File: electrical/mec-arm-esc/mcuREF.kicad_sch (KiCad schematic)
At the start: 15 parts, among them SW1 SH-1808SN-250GF, SW2 SH-1808SN-250GF, U2 STM32G474RET3

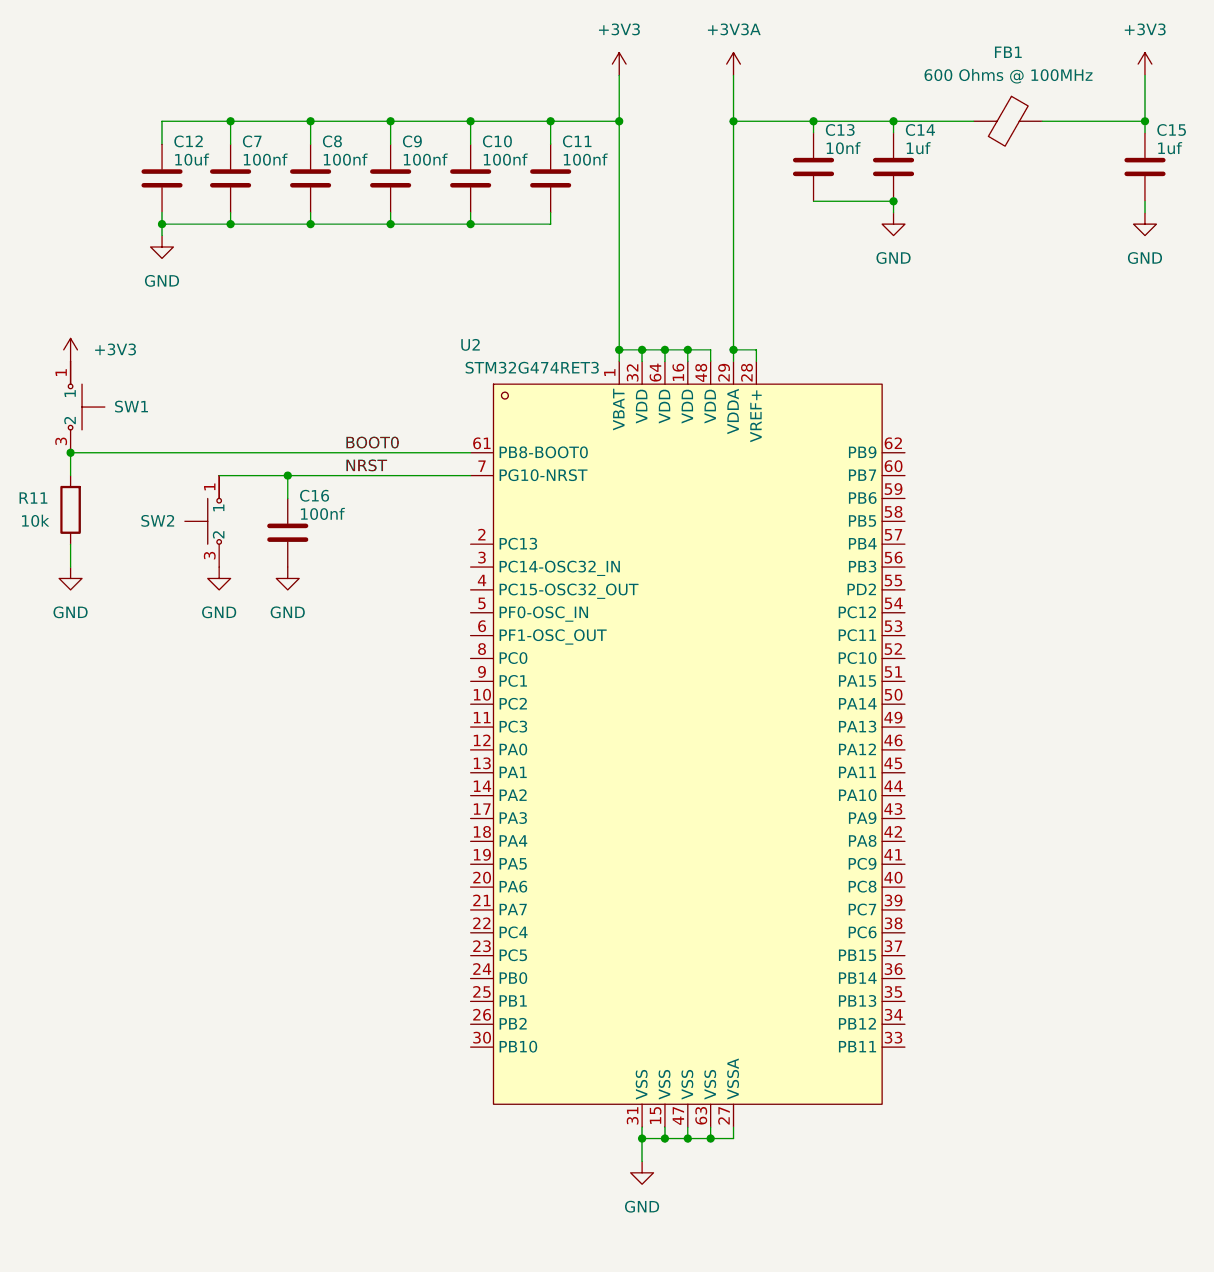
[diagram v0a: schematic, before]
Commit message: updated arm with proper basic mcu routing
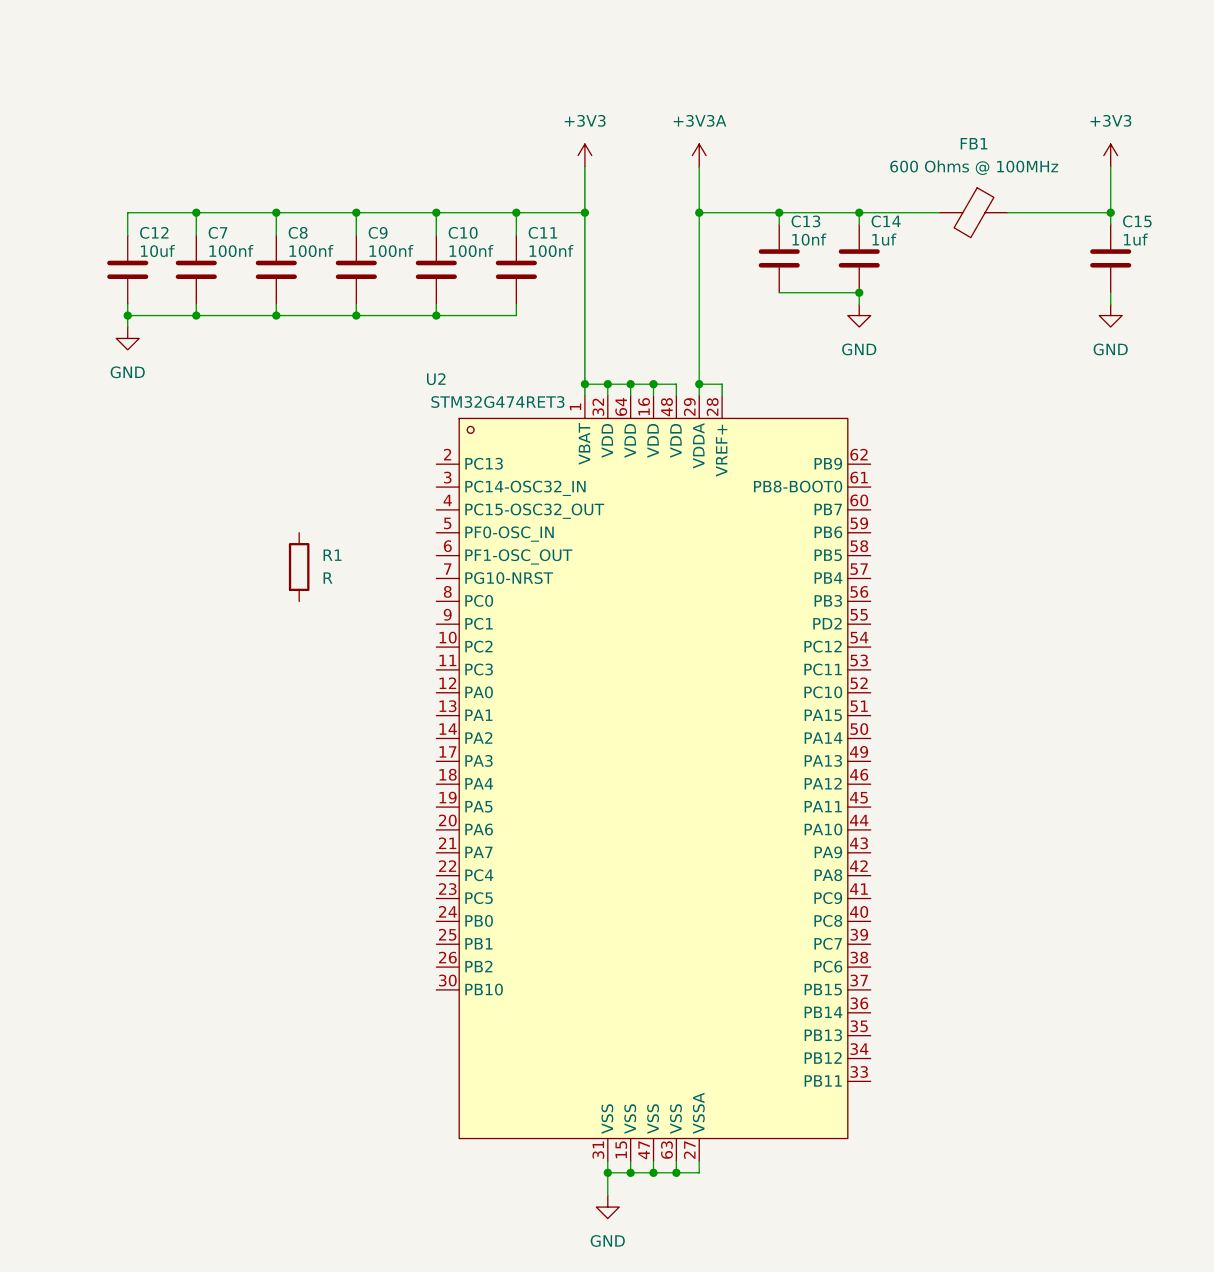
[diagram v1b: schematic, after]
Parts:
- removed C16: 100nf, symbol Device:C
- removed R11: 10k, symbol Device:R
- removed SW1, SW2: SH-1808SN-250GF, EasyEDA:SW-SMD_4P-L4.2-W3.4-P2.15-LS5.2, symbol core:SH-1808SN-250GF
- added R1: R, symbol Device:R
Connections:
- net BOOT0: no longer names the net of U2.61 (PB8-BOOT0)
- net NRST: no longer names the net of U2.7 (PG10-NRST)
